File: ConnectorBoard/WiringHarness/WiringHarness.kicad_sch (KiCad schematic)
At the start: 37 parts, among them J1 Barrel_Jack, J2 Conn_01x03, J3 Conn_01x03, J4 Conn_02x05_Odd_Even, J5 Socket, J6 Qwiic, J7 Header, U1 PCA9306DQER, U2 TLV75533PDBV, U3 NCP1117-ADJ_SOT223

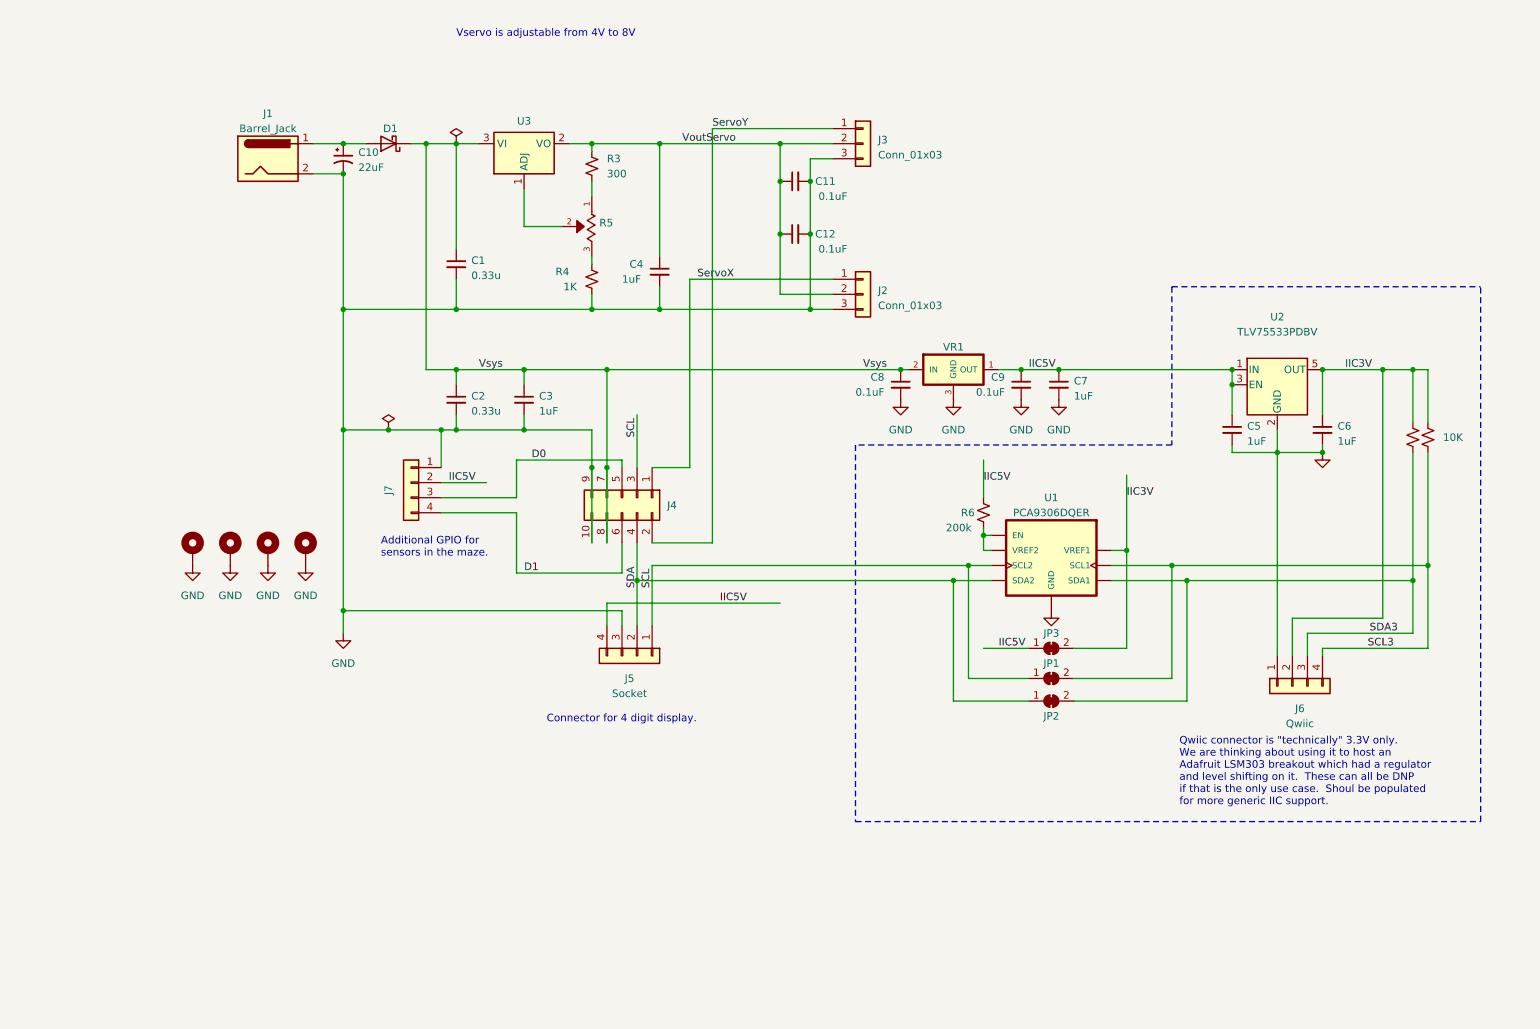
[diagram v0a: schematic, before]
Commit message: add some docs
Convert to STM32C031 based stepper version.
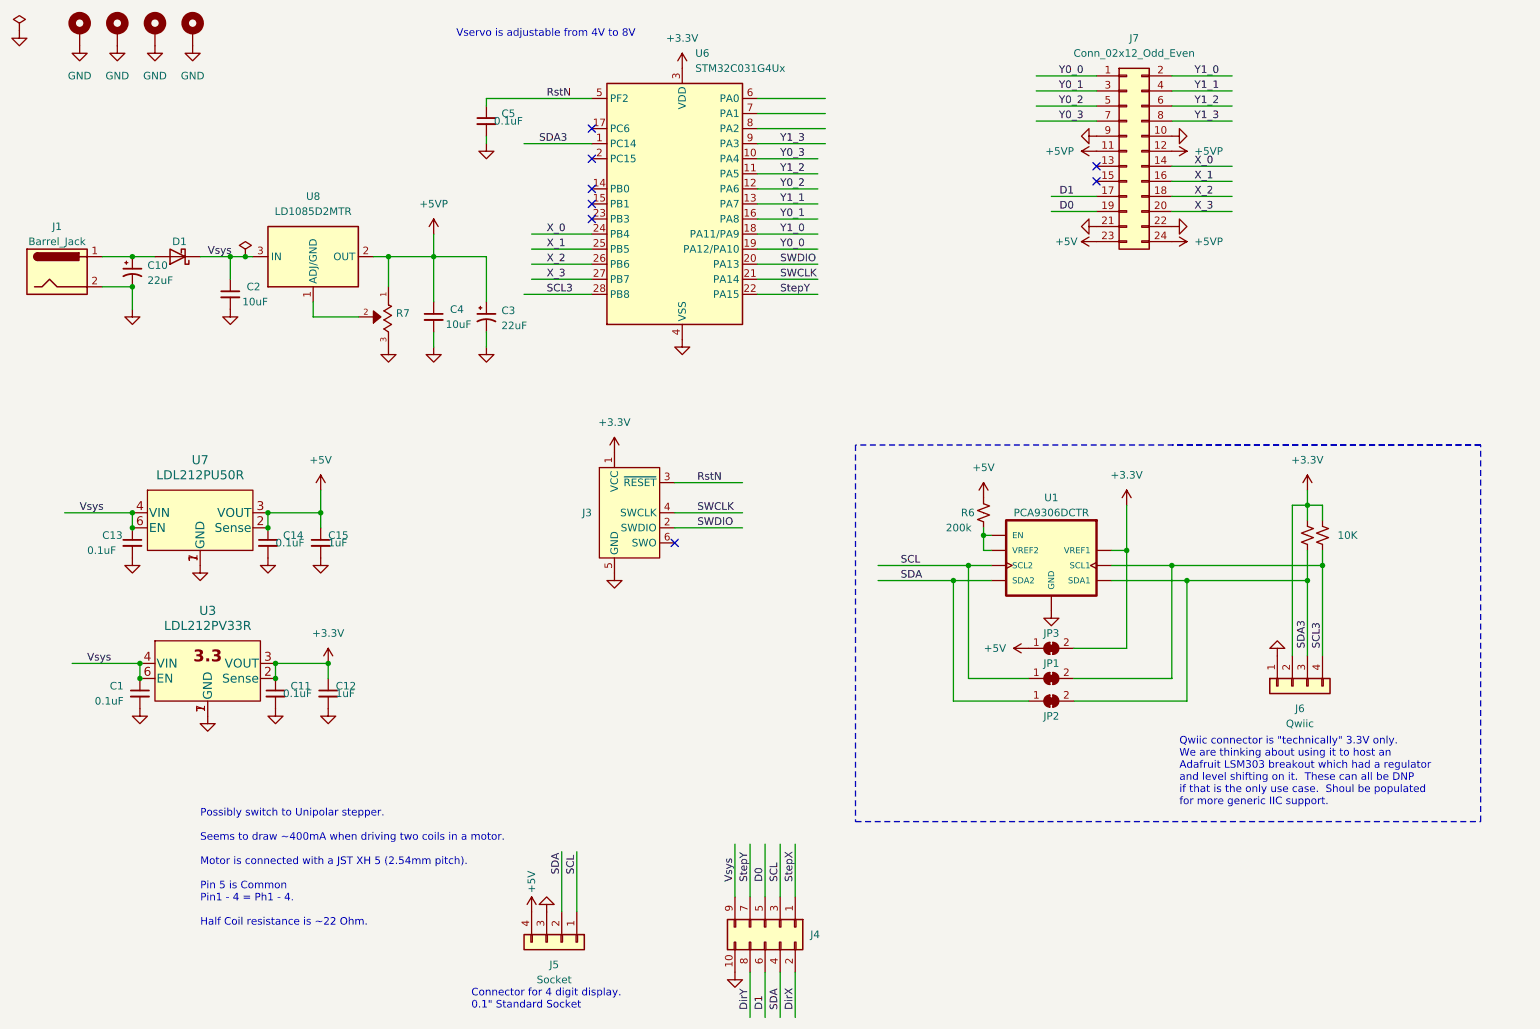
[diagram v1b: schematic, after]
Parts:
- removed C3, C6, C7: 1uF, Capacitor_SMD:C_0603_1608Metric, symbol Device:C_Small
- removed C8, C9: 0.1uF, Capacitor_SMD:C_0603_1608Metric, symbol Device:C_Small
- removed J2, J3: Conn_01x03, Connector_PinHeader_2.54mm:PinHeader_1x03_P2.54mm_Horizontal, symbol Connector_Generic:Conn_01x03
- removed J7: Header, Connector_JST:JST_PH_S4B-PH-K_1x04_P2.00mm_Horizontal, symbol Connector_Generic:Conn_01x04
- removed R3: 300, Resistor_SMD:R_0603_1608Metric, symbol Device:R_Small_US
- removed R4: 1K, Resistor_SMD:R_0603_1608Metric, symbol Device:R_Small_US
- removed R5: TC33X-2-201E, Passives:TRIM_TC33X-2-201E, symbol StockedComponents:TC33X-2-201E
- removed U2: TLV75533PDBV, Package_TO_SOT_SMD:SOT-23-5, symbol Regulator_Linear:TLV75533PDBV
- removed U3: NCP1117-ADJ_SOT223, Package_TO_SOT_SMD:SOT-223-3_TabPin2, symbol Regulator_Linear:NCP1117-ADJ_SOT223
- removed VR1: TLV76050DBZR, TexasInstruments:SOT95P237X112-3N, symbol StockedComponents:TLV76050DBZR
- added C13, C14: 0.1uF, Capacitor_SMD:C_0603_1608Metric, symbol Device:C_Small
- added C15: 1uF, Capacitor_SMD:C_0603_1608Metric, symbol Device:C_Small
- added C3: 22uF, Capacitor_THT:CP_Radial_D6.3mm_P2.50mm, symbol Device:C_Polarized_Small_US
- added J3: Conn_ARM_SWD_TagConnect_TC2030-NL, Connector:Tag-Connect_TC2030-IDC-NL_2x03_P1.27mm_Vertical, symbol Connector:Conn_ARM_SWD_TagConnect_TC2030-NL
- added J7: Conn_02x12_Odd_Even, Connector_PinHeader_2.54mm:PinHeader_2x12_P2.54mm_Horizontal, symbol Connector_Generic:Conn_02x12_Odd_Even
- added R7: TC33X-2-102E, Passives:TRIM_TC33X-2-201E, symbol StockedComponents:TC33X-2-201E
- added U3: LDL212PV33R, STMicro:LDL212_2x2mm_Pitch0.5mm, symbol StockedComponents:LDL212PV33R
- added U6: STM32C031G4Ux, Package_DFN_QFN:QFN-28_4x4mm_P0.5mm, symbol MCU_ST_STM32C0:STM32C031G4Ux
- added U7: LDL212PU50R, STMicro:LDL212_3x3mm_Pitch0.95mm, symbol StockedComponents:LDL212PU50R
- added U8: LD1085D2MTR, Package_TO_SOT_SMD:TO-263-3_TabPin2, symbol Regulator_Linear:LD1086D2MTR
- C1: value 0.33u -> 0.1uF; Digikey TAJR334K020RNJ -> 1276-1861-1-ND; Vendor 445-5950-1-ND -> 1276-1861-1-ND
- C11: Digikey (none) -> 1276-1861-1-ND; Vendor (none) -> 1276-1861-1-ND
- C12: value 0.1uF -> 1uF; Digikey (none) -> 1276-1861-1-ND; Vendor (none) -> 1276-1861-1-ND
- C2: value 0.33u -> 10uF; footprint Capacitor_SMD:C_0603_1608Metric -> Capacitor_SMD:C_0805_2012Metric; Digikey TAJR334K020RNJ -> 490-10500-1-ND; Vendor 445-5950-1-ND -> 490-10500-1-ND
- C4: value 1uF -> 10uF; footprint Capacitor_SMD:C_0603_1608Metric -> Capacitor_SMD:C_0805_2012Metric; Digikey 1276-1861-1-ND -> 490-10500-1-ND; Vendor 1276-1861-1-ND -> 490-10500-1-ND
- C5: value 1uF -> 0.1uF
- R6: Digikey (none) -> RMCF0603FT200KCT-ND; Vendor (none) -> RMCF0603FT200KCT-ND
- U1: value PCA9306DQER -> PCA9306DCTR; footprint Package_SO:TSSOP-8_3x3mm_P0.65mm -> Package_SO:MSOP-8_3x3mm_P0.65mm; Digikey (none) -> 296-18509-1-ND; Vendor (none) -> 296-18509-1-ND
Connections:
- net D0: now also J7.19 (Pin_19)
- net D1: now also J7.17 (Pin_17)
- net GND: now also C13.2, C14.2, C15.2, C3.2, J3.5 (GND), J7.10 (Pin_10), J7.21 (Pin_21), J7.22 (Pin_22), J7.9 (Pin_9), R7.3, U3.1 (GND), U3.7 (GND), U6.4 (VSS), U7.1 (GND), U7.7 (GND); no longer J4.9 (Pin_9)
- net SCL3: now also U6.28 (PB8)
- net SDA3: now also U6.1 (PC14)
- net Vsys: now also J4.9 (Pin_9), C13.1, U3.4 (VIN), U3.6 (EN), U7.4 (VIN), U7.6 (EN), U8.3 (IN); no longer J4.7 (Pin_7), J4.8 (Pin_8)
- net IIC3V renamed +3.3V
- net +3.3V: now also C11.1, C12.1, J3.1 (VCC), U3.2 (Sense), U3.3 (VOUT), U6.3 (VDD)
- net IIC5V renamed +5V
- net +5V: now also C14.1, C15.1, J7.23 (Pin_23), U7.2 (Sense), U7.3 (VOUT); no longer C5.1
- net ServoX renamed StepX
- net ServoY renamed DirX
- removed net VoutServo: C11.1, C12.1, C4.1
- new net: R7.2, U8.1 (ADJ/GND)
- new net +5VP: C3.1, C4.1, J7.11 (Pin_11), J7.12 (Pin_12), J7.24 (Pin_24), R7.1, U8.2 (OUT)
- new net DirY: J4.8 (Pin_8)
- new net RstN: C5.1, J3.3 (~{RESET}), U6.5 (PF2)
- new net SWCLK: J3.4 (SWCLK), U6.21 (PA14)
- new net SWDIO: J3.2 (SWDIO), U6.20 (PA13)
- new net StepY: J4.7 (Pin_7), U6.22 (PA15)
- new net X_0: J7.14 (Pin_14), U6.24 (PB4)
- new net X_1: J7.16 (Pin_16), U6.25 (PB5)
- new net X_2: J7.18 (Pin_18), U6.26 (PB6)
- new net X_3: J7.20 (Pin_20), U6.27 (PB7)
- new net Y0_0: J7.1 (Pin_1), U6.19 (PA12/PA10)
- new net Y0_1: J7.3 (Pin_3), U6.16 (PA8)
- new net Y0_2: J7.5 (Pin_5), U6.12 (PA6)
- new net Y0_3: J7.7 (Pin_7), U6.10 (PA4)
- new net Y1_0: J7.2 (Pin_2), U6.18 (PA11/PA9)
- new net Y1_1: J7.4 (Pin_4), U6.13 (PA7)
- new net Y1_2: J7.6 (Pin_6), U6.11 (PA5)
- new net Y1_3: J7.8 (Pin_8), U6.9 (PA3)
- no-connect marks 0 -> 8
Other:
- note added: "Connector for 4 digit display. 0.1" Standard Socket"
- note added: "Possibly switch to Unipolar stepper. Seems to draw ~400mA when driving two coils in a motor. Motor is connected with a JST XH 5 (2.54mm pitch). Pin 5 is Common Pin1 - 4 = Ph1 - 4. Half Coil resistance is ~22 Ohm."
- note removed: "Additional GPIO for sensors in the maze."
- note removed: "Connector for 4 digit display."
- moved on the sheet: C10, C4, D1, J1, J4, J5

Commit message: fully connected and drc clean.  Need to examine copper pours
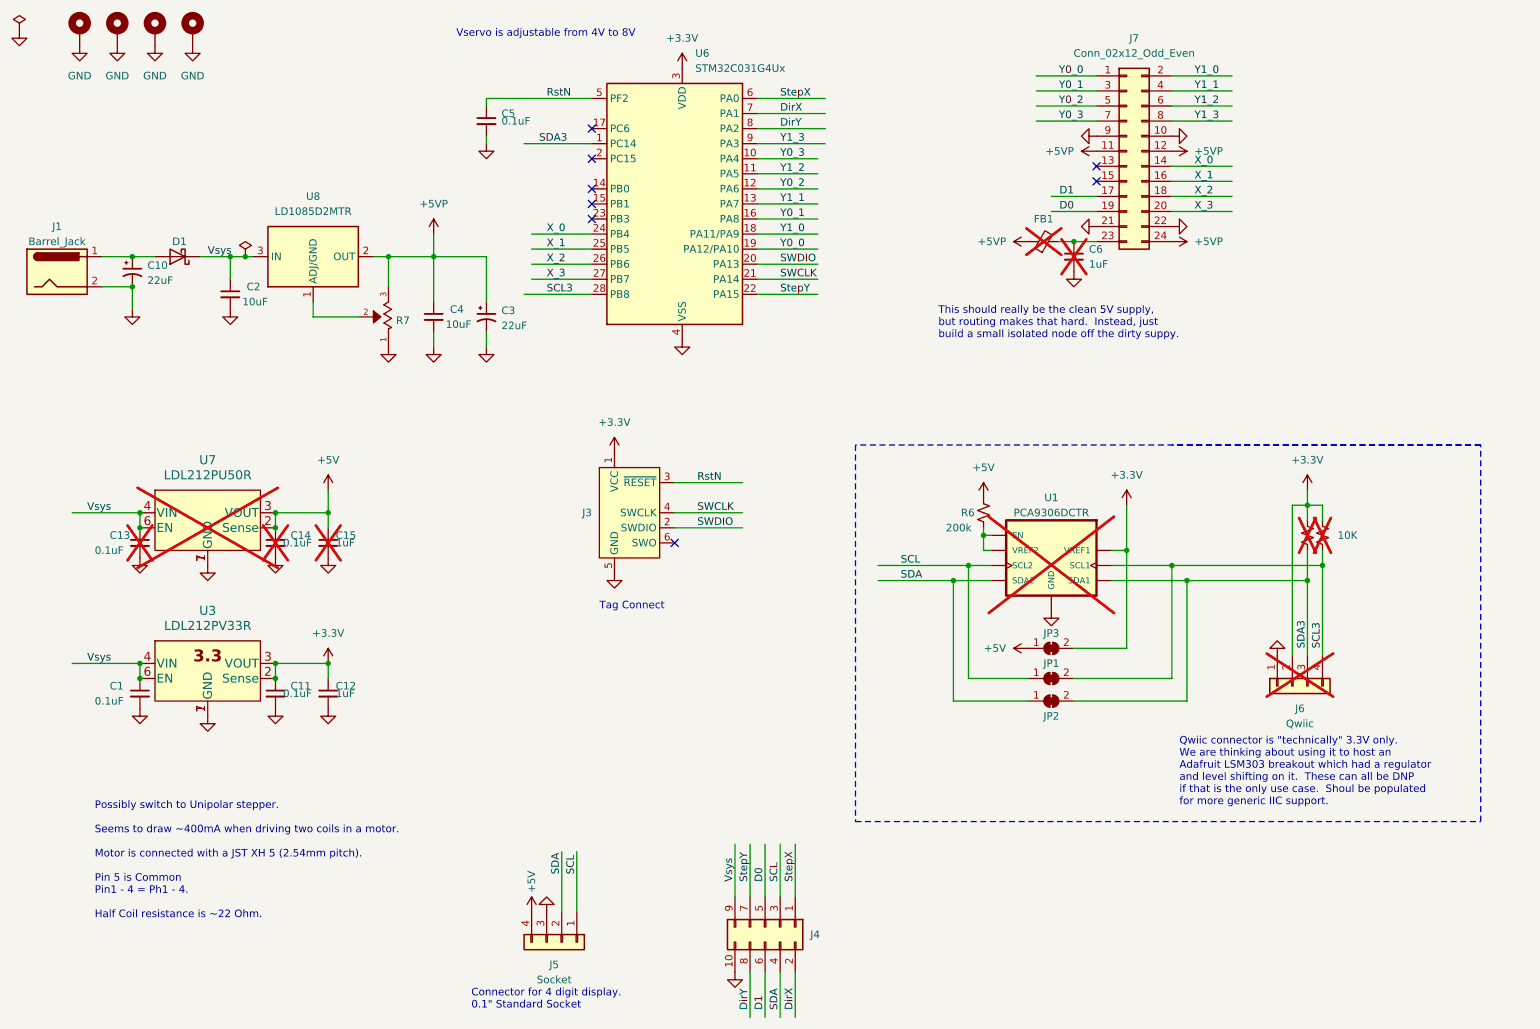
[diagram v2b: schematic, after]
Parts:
- added C6: C_1U, Capacitor_SMD:C_0603_1608Metric, symbol StockedComponents:C_1U
- added FB1: FB_120_100MHz, Inductor_SMD:L_0603_1608Metric, symbol StockedComponents:FB_120_100MHz
- C13, C14, C15, J6, R1, R2, U1, U7: now not fitted
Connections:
- net +5V: no longer J7.23 (Pin_23)
- net +5VP: now also R7.3, FB1.1; no longer R7.1
- net DirX: now also U6.7 (PA1)
- net DirY: now also U6.8 (PA2)
- net GND: now also R7.1, C6.2; no longer R7.3
- net StepX: now also U6.6 (PA0)
- new net: C6.1, FB1.2, J7.23 (Pin_23)
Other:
- note added: "Tag Connect"
- note added: "This should really be the clean 5V supply, but routing makes that hard. Instead, just build a small isolated node off the dirty suppy."

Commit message: Fix #19 - no artwork changes
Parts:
- U3: Digikey 497-16898-1-ND -> 497-19548-1-ND; Vendor 497-16898-1-ND -> 497-19548-1-ND
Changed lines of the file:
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@@
       (effects (font (size 1.524 1.524)))
     )
-    (property "Digikey" "497-16898-1-ND" (at 35.56 130.81 0)
+    (property "Digikey" "497-19548-1-ND" (at 35.56 130.81 0)
       (effects (font (size 1.27 1.27)) hide)
     )
-    (property "Vendor" "497-16898-1-ND" (at 35.56 130.81 0)
+    (property "Vendor" "497-19548-1-ND" (at 35.56 130.81 0)
       (effects (font (size 1.27 1.27)) hide)
     )
